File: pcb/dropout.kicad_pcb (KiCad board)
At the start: 2 copper layers, 226.7 x 94.4 mm, 61 parts, among them SW1 Rotary_Encoder_Switch, SW2 SW_Push, U1 ProMicro

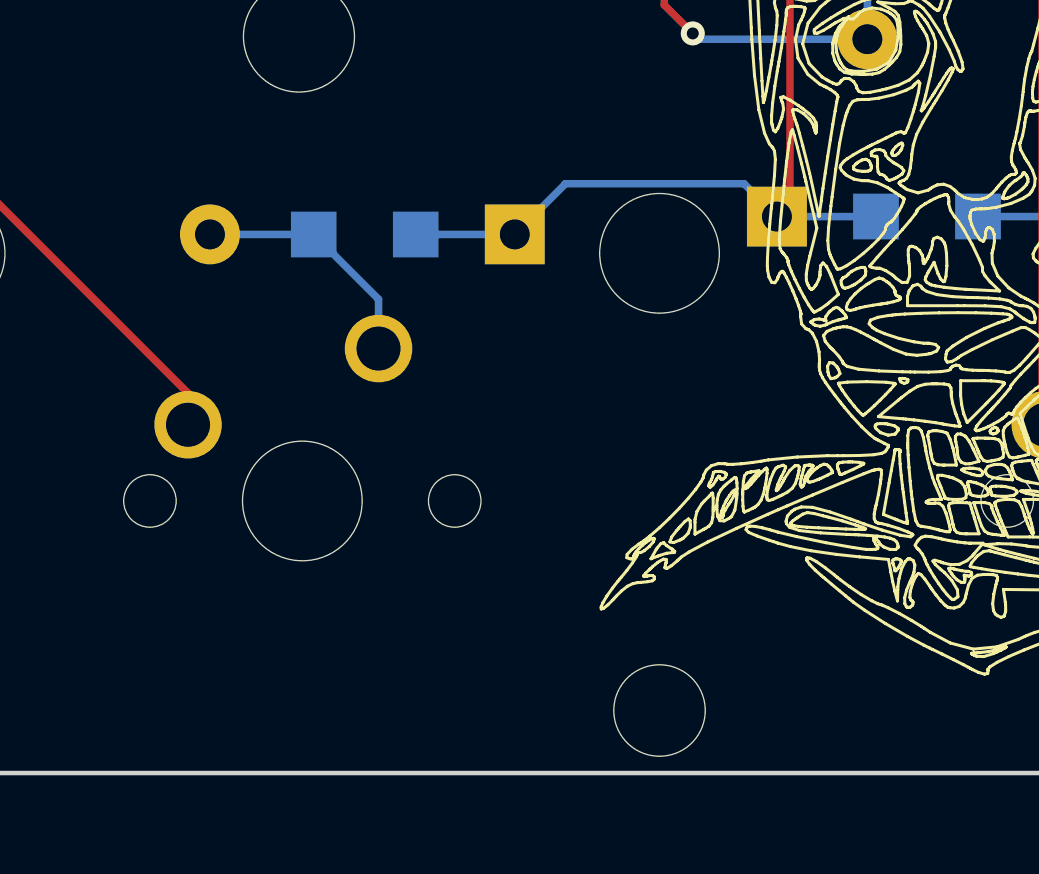
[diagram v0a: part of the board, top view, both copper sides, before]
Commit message: moving diodes to stop interference with stabilizer
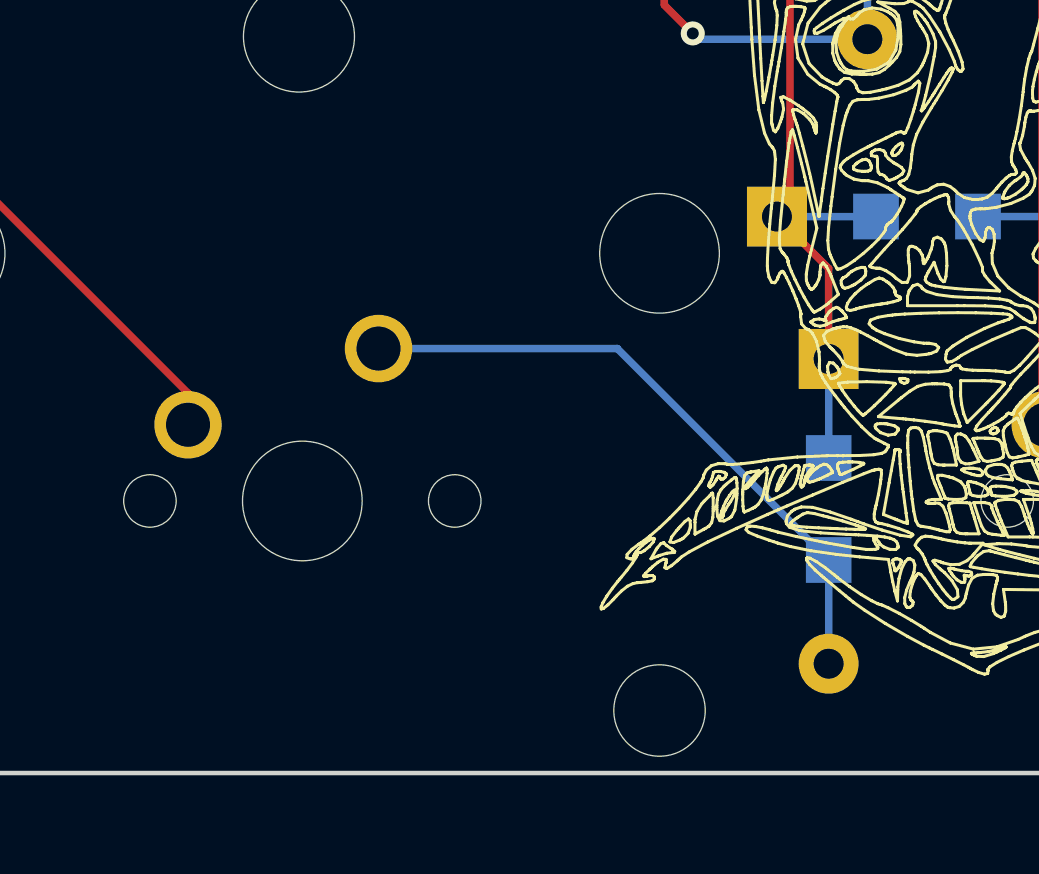
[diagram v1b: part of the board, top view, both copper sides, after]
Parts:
- moved D5 11.3 mm to (173.7, 130.9), turned to 270 degrees
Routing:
- net Net-(D5-Pad2): track 8.16 -> 21.4 mm
- net ROW4: track 68.1 -> 63.6 mm

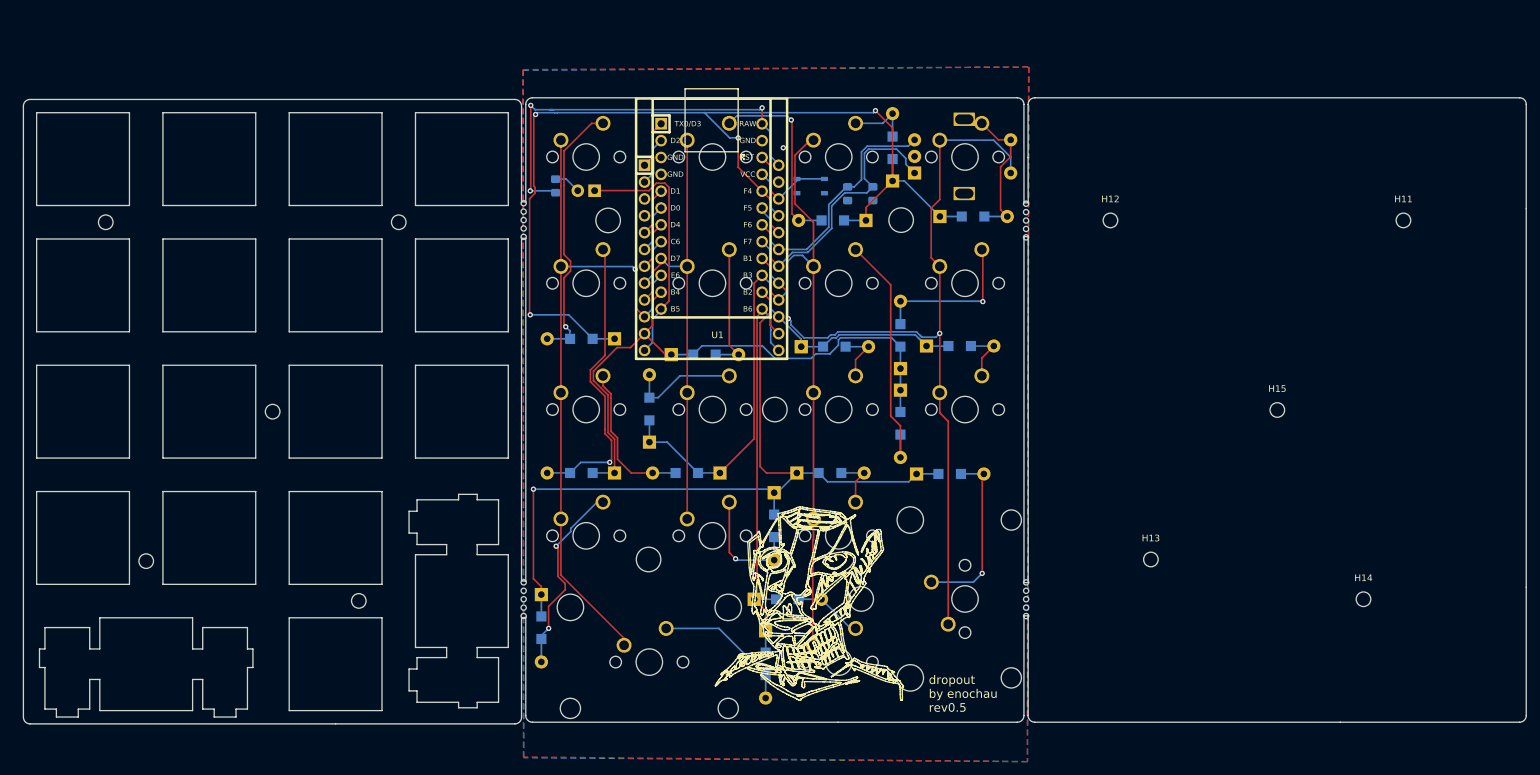
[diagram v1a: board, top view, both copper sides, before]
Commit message: flipping orientation of promicro for better clearance, now uses same pinout as rev0.1
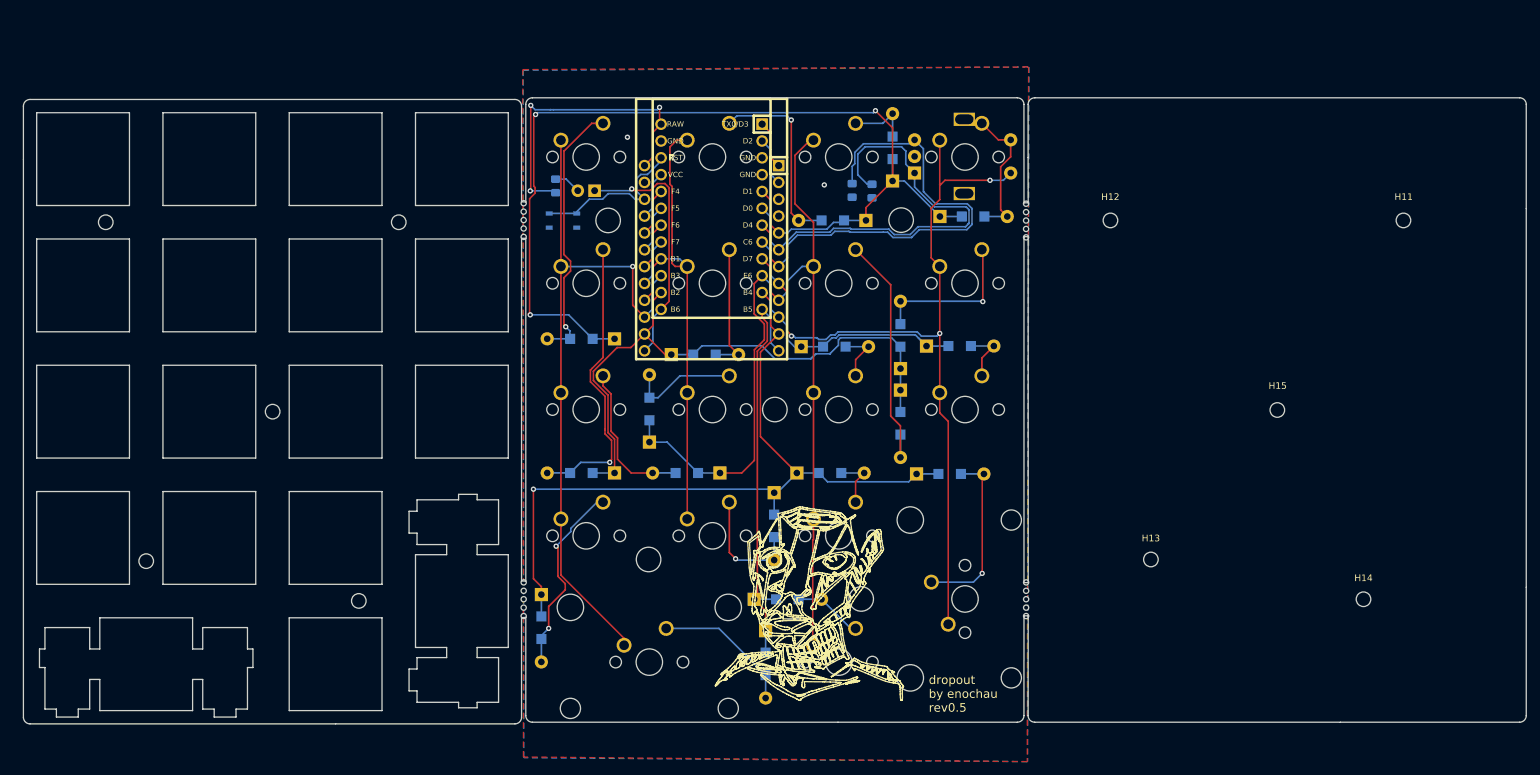
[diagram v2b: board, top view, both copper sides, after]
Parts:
- U1: moved to B.Cu
- moved SW2 37.7 mm to (143.2, 69.1)
- moved U1 1.20 mm to (165.0, 69.2)
- moved C1 0.85 mm to (186.8, 64.5)
- moved C2 0.42 mm to (189.8, 64.6)
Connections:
- U1 pad 10: COL0 -> ROW2
- U1 pad 11: ROW1 -> ROW3
- U1 pad 12: NUMLED -> ROW4
- U1 pad 13: ROW4 -> NUMLED
- U1 pad 14: ROW3 -> ROW1
- U1 pad 15: ROW2 -> COL0
- U1 pad 16: COL2 -> COL1
- U1 pad 17: COL3 -> Net-(U1-Pad17)
- U1 pad 18: ROT-A -> Net-(U1-Pad18)
- U1 pad 19: ROT-B -> Net-(U1-Pad19)
- U1 pad 20: ROW0 -> Net-(U1-Pad20)
- U1 pad 5: Net-(U1-Pad5) -> ROW0
- U1 pad 6: Net-(U1-Pad6) -> ROT-A
- U1 pad 7: Net-(U1-Pad7) -> ROT-B
- U1 pad 8: Net-(U1-Pad8) -> COL3
- U1 pad 9: COL1 -> COL2
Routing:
- net ROT-B: track 39.1 -> 74.8 mm
- net ROT-A: track 43.9 -> 70.9 mm
- net +5V: track 62.7 -> 46.7 mm
- net Net-(SW2-Pad2): track 15.6 -> 25.0 mm
- net Net-(U1-Pad8): track 7.29 -> 0.00 mm
- net Net-(U1-Pad7): track 7.29 -> 0.00 mm
- net Net-(U1-Pad6): track 7.29 -> 0.00 mm
- net Net-(U1-Pad5): track 7.29 -> 0.00 mm
- net Net-(U1-Pad20): track 0.00 -> 7.29 mm
- net Net-(U1-Pad19): track 0.00 -> 7.29 mm
- net Net-(U1-Pad18): track 0.00 -> 7.29 mm
- net Net-(U1-Pad17): track 0.00 -> 7.29 mm
- net ROW3: track 124.0 -> 118.5 mm
- net ROW0: track 158.8 -> 153.2 mm, vias 4 -> 3
- net COL1: track 68.9 -> 73.0 mm
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
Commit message: adding graphics to pcb, some cleanup
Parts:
- added G***: LOGO, graphics:yosemite_topo_map, F.Cu at (98.7, 97.5)
- added G***: LOGO, graphics:kenzo_speechless_invert, F.Cu at (273.9, 134.7)
- added G***: LOGO, graphics:miffy, B.Cu at (250.9, 77.7)
- added G***: LOGO, graphics:me_big, F.Cu at (179.6, 128.2)
-  : renamed from H15
-  : renamed from H14
-  : renamed from H13
-  : renamed from H12
-  : renamed from H11
- moved C1 0.35 mm to (187.1, 64.5)

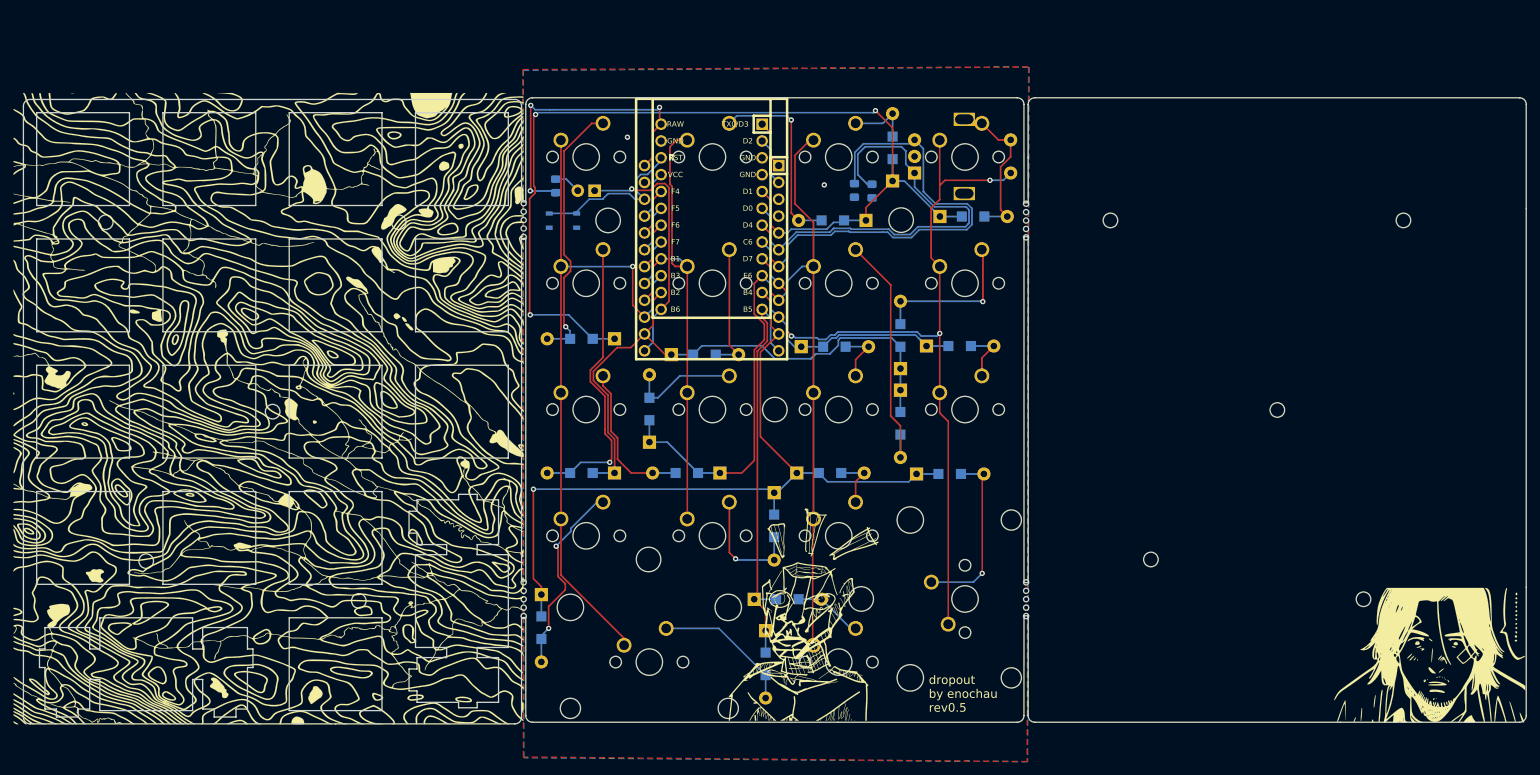
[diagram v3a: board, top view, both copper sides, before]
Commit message: breaking up panelization for production
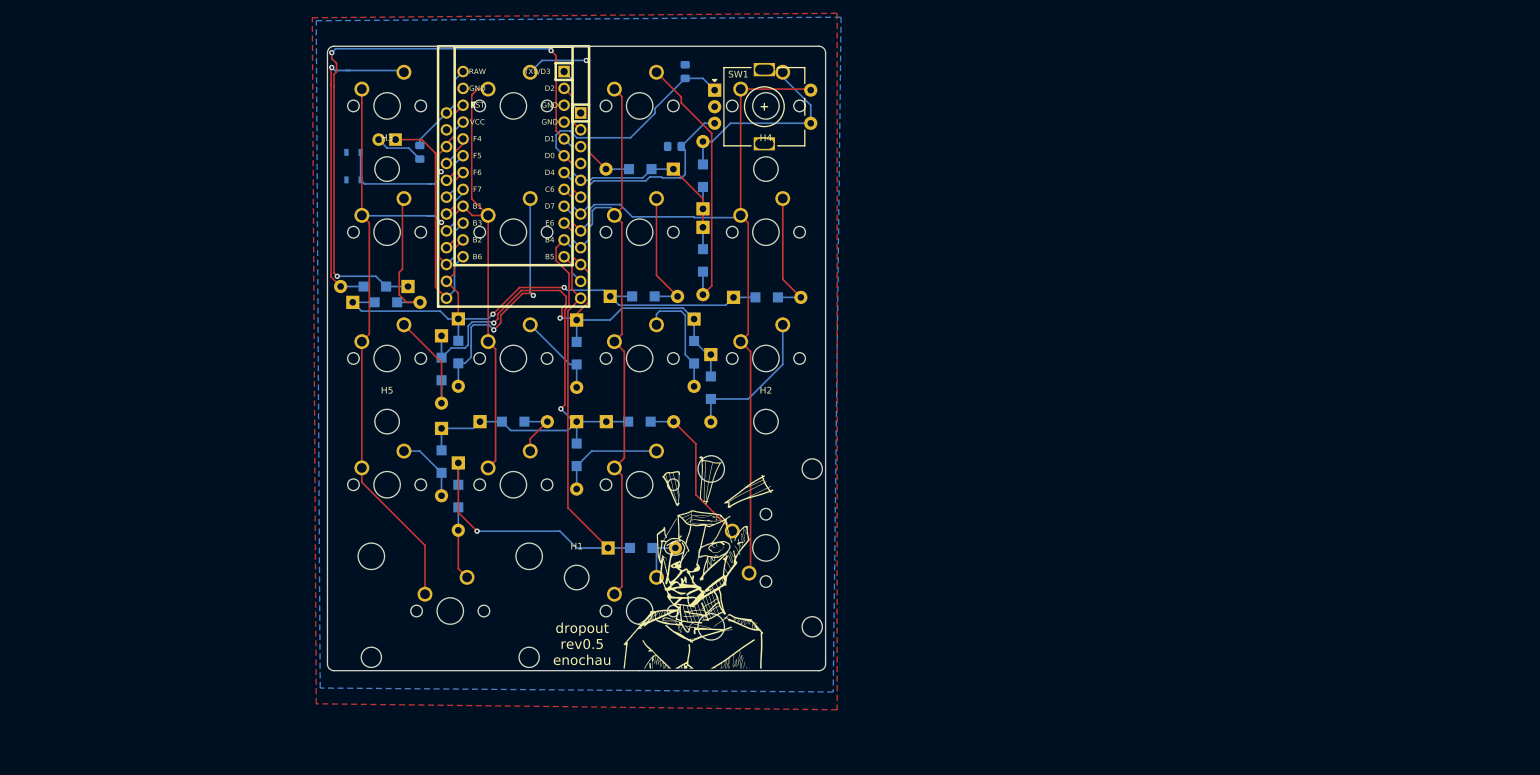
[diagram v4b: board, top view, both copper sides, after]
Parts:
- removed  : MountingHole, MountingHole:MountingHole_2.2mm_M2 (x5)
- removed the G*** at (98.7, 97.5)
- removed the G*** at (273.9, 134.7)
- removed the G*** at (250.9, 77.7)
- removed H10, H6, H7, H8, H9: MountingHole, MountingHole:MountingHole_2.2mm_M2
- removed H16, H17, H18, H19: mouse-bites, Keebio-Parts:breakaway-mousebites
- D1, D10, D11, D12, D13, D14, D15, D16, D17, D18, D2, D3, D4, D5, D6, D7, D8, D9: footprint footprint:Diode_TH_SOD123 -> Diodes_SMD:Diode_TH_SOD123
- SW1: moved to F.Cu
- moved H3 68.8 mm to (116.6, 61.3)
- moved H4 66.4 mm to (173.8, 61.3)
- moved D5 52.8 mm to (127.4, 105.6)
- moved D18 47.5 mm to (149.7, 99.4)
- moved D2 47.1 mm to (111.4, 81.4), turned to 0 degrees
- moved D3 46.8 mm to (124.8, 86.5), turned to 270 degrees
- moved D11 46.0 mm to (150.3, 80.5), turned to 0 degrees
- moved D9 45.7 mm to (130.6, 99.4), turned to 0 degrees
- moved H5 45.1 mm to (116.6, 99.4)
- moved H2 36.6 mm to (173.8, 99.4)
- moved D15 35.8 mm to (164.3, 67.3), turned to 90 degrees
- moved D13 34.1 mm to (145.2, 99.4), turned to 270 degrees
- moved C2 33.5 mm to (161.6, 46.6), turned to 90 degrees
- moved SW1 32.7 mm to (166.0, 49.4)
- moved SW2 32.6 mm to (111.6, 60.9), turned to 270 degrees
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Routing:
- net ROW3: track 118.5 -> 74.0 mm
- net ROT-B: track 74.7 -> 38.6 mm
- net +5V: track 46.7 -> 13.9 mm, vias 3 -> 0
- net Net-(D10-Pad2): track 9.65 -> 41.0 mm
- net ROT-A: track 70.9 -> 40.4 mm
- net Net-(D2-Pad2): track 44.8 -> 21.9 mm, vias 1 -> 0
- net ROW4: track 64.8 -> 87.2 mm, vias 0 -> 1
- net ROW0: track 153.2 -> 133.3 mm
- net Net-(D4-Pad2): track 29.6 -> 10.5 mm, vias 2 -> 0
- net Net-(D7-Pad2): track 19.9 -> 38.0 mm, vias 0 -> 2
- net Net-(D11-Pad2): track 37.6 -> 19.5 mm
- net Net-(D17-Pad2): track 8.71 -> 22.4 mm
- net Net-(D5-Pad2): track 21.4 -> 11.1 mm
- net Net-(D15-Pad2): track 21.4 -> 31.1 mm
- net Net-(D9-Pad2): track 18.3 -> 8.96 mm, vias 1 -> 0
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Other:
- board size 226.7 x 94.4 mm -> 75.1 x 94.2 mm
- board text added: "dropout rev0.5 enochau"
- board text removed: "dropout by enochau rev0.5"
